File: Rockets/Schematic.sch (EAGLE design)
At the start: 9 parts, among them IC1 LM2937

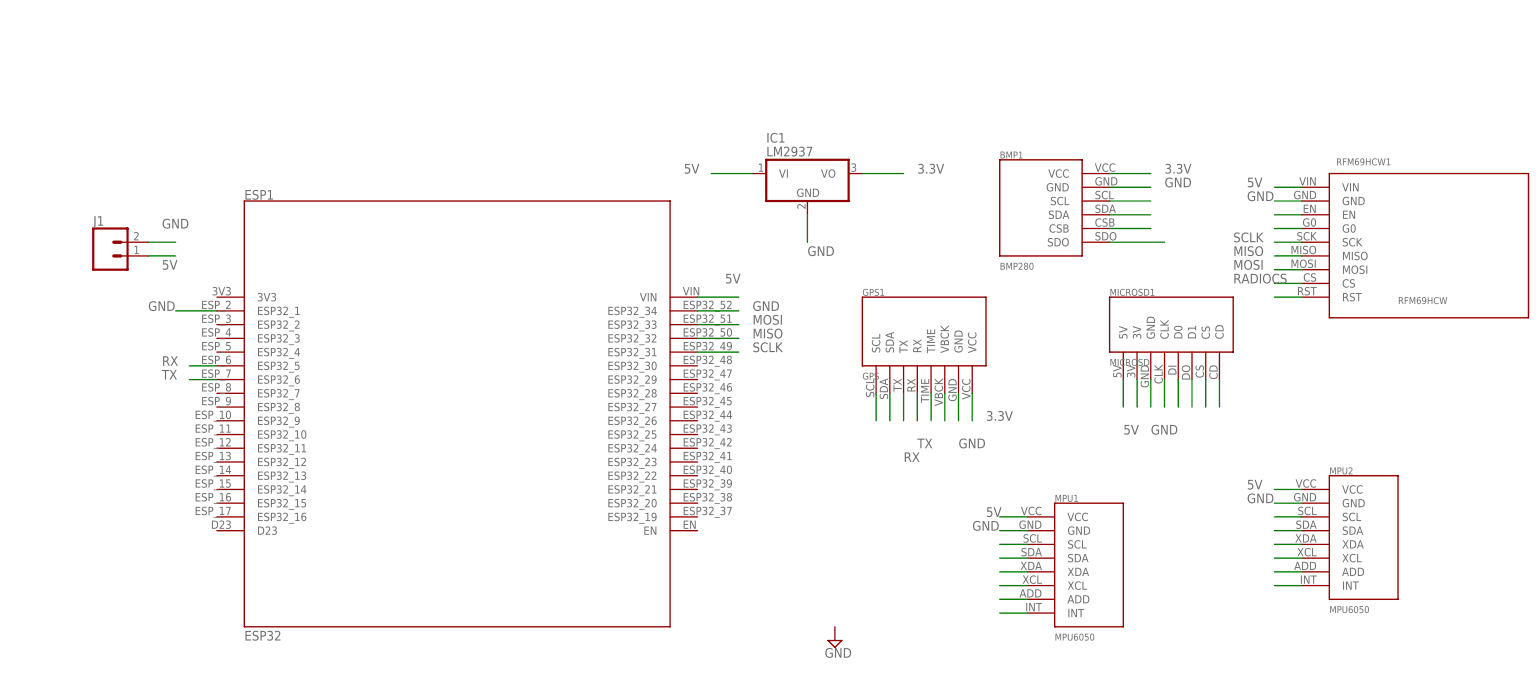
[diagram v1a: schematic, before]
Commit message: Everthing added needs resistors
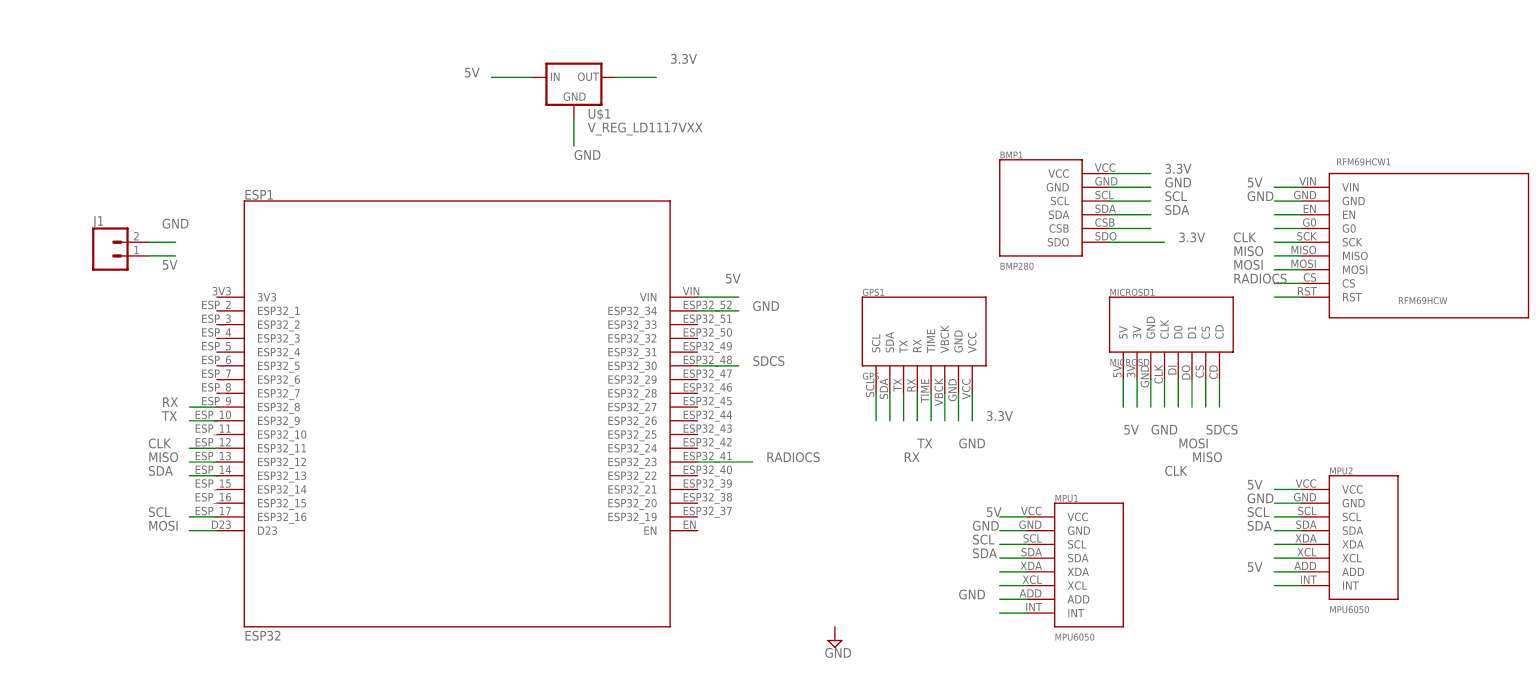
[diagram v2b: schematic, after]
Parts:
- removed IC1: LM2937, linear:LM2937
- added U$1: V_REG_LD1117VXX, SparkFun-IC-Power:V_REG_LD1117VXX
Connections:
- removed net N$19: MICROSD1.CS
- removed net N$20: MICROSD1.D1
- removed net N$21: MICROSD1.CLK
- removed net N$22: MICROSD1.D0
- removed net N$23: MPU1.SCL
- removed net N$26: MPU1.SDA
- removed net N$29: MPU1.ADD
- removed net N$33: MPU2.SCL
- removed net N$34: MPU2.SDA
- removed net N$38: MPU2.ADD
- removed net N$5: BMP1.SCL
- removed net N$6: BMP1.SDA
- removed net N$8: BMP1.SDO
- removed net SCLK: ESP1.ESP32_31, RFM69HCW1.SCK
- new net CLK: ESP1.ESP32_11, MICROSD1.CLK, RFM69HCW1.SCK
- new net SCL: BMP1.SCL, ESP1.ESP32_16, MPU1.SCL, MPU2.SCL
- new net SDA: BMP1.SDA, ESP1.ESP32_13, MPU1.SDA, MPU2.SDA
- new net SDCS: ESP1.ESP32_30, MICROSD1.CS
- net 3.3V: now also BMP1.SDO, U$1.OUT; no longer IC1.VO
- net 5V: now also MPU2.ADD, U$1.IN; no longer IC1.VI
- net GND: now also MPU1.ADD, U$1.GND; no longer ESP1.ESP32_1, IC1.GND
- net MISO: now also ESP1.ESP32_12, MICROSD1.D1; no longer ESP1.ESP32_32
- net MOSI: now also ESP1.D23, MICROSD1.D0; no longer ESP1.ESP32_33
- net RADIOCS: now also ESP1.ESP32_23
- net RX: now also ESP1.ESP32_8; no longer ESP1.ESP32_5
- net TX: now also ESP1.ESP32_9; no longer ESP1.ESP32_6

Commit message: Mk1 completed?
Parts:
- removed RFM69HCW1: RFM69HCW, awesome:RFM69HCW
- added C1, C2, C3, C4, C5, C6: 0.1uF, SparkFun-Capacitors:0.1UF-KIT-EZ-50V-20%
- added D1: (no value), SparkFun-LED:LED-3MM-NO_SILK
- added R1, R2, R3, R4, R5, R7: (no value), SparkFun-Resistors:RESISTORAXIAL-0.3
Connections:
- removed net N$18: MICROSD1.CD
- removed net N$9: RFM69HCW1.RST
- new net N$1: ESP1.ESP32_11, R3.1
- new net N$2: D1.A, ESP1.ESP32_27
- new net SDCD: ESP1.ESP32_24, MICROSD1.CD
- net 3.3V: now also C4.1, C6.1, R1.2, R7.2
- net 5V: now also C1.1, C2.1, C3.2, C5.2; no longer RFM69HCW1.VIN
- net CLK: now also R3.2; no longer ESP1.ESP32_11, RFM69HCW1.SCK
- net GND: now also C1.2, C2.2, C3.1, C4.2, C5.1, C6.2, R4.1; no longer RFM69HCW1.GND
- net MISO: now also R5.2; no longer MICROSD1.D1, RFM69HCW1.MISO
- net MOSI: now also R2.1, R2.2; no longer RFM69HCW1.MOSI
- net N$3: now also D1.C, R4.2; no longer RFM69HCW1.EN
- net N$4: now also MICROSD1.D1, R5.1; no longer RFM69HCW1.G0
- net RADIOCS: no longer RFM69HCW1.CS
- net SCL: now also R1.1
- net SDA: now also R7.1
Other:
- moved on the sheet: ESP1, GPS1

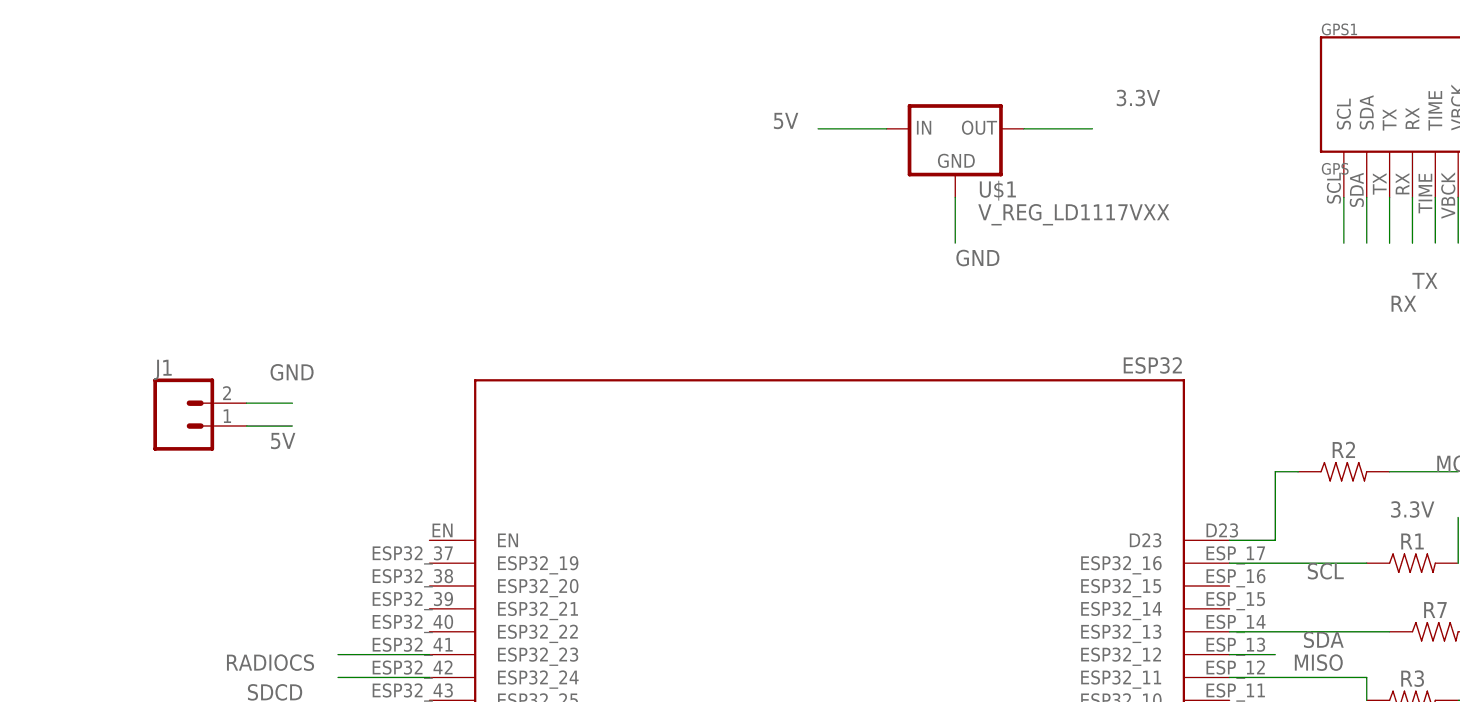
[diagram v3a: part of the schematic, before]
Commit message: Updated the schematics from discord zip
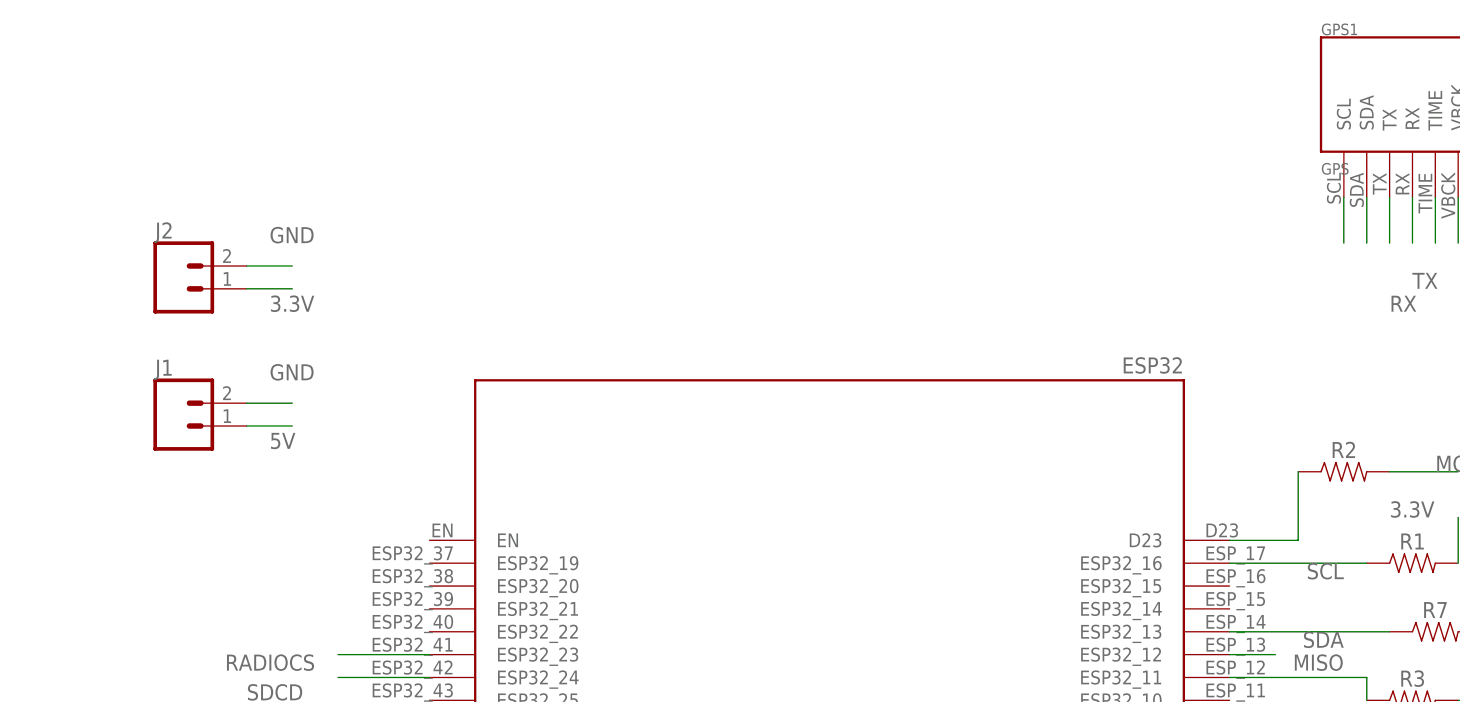
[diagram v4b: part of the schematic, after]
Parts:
- removed U$1: V_REG_LD1117VXX, SparkFun-IC-Power:V_REG_LD1117VXX
- added J2: (no value), SparkFun-Connectors:CONN_02
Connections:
- new net N$5: ESP1.D23, R2.1
- net 3.3V: now also J2.1; no longer U$1.OUT
- net 5V: no longer U$1.IN
- net GND: now also J2.2; no longer U$1.GND
- net MOSI: no longer ESP1.D23, R2.1
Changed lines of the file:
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@@
 <part name="J1" library="SparkFun-Connectors" deviceset="CONN_02" device=""/>
 <part name="BMP1" library="awesome" deviceset="BMP280" device=""/>
-<part name="U$1" library="SparkFun-IC-Power" deviceset="V_REG_LD1117VXX" device=""/>
 <part name="D1" library="SparkFun-LED" deviceset="LED" device="-3MM-NO_SILK"/>
 <part name="R1" library="SparkFun-Resistors" deviceset="RESISTOR" device="AXIAL-0.3" value=" "/>
@@
 <part name="R4" library="SparkFun-Resistors" deviceset="RESISTOR" device="AXIAL-0.3" value=" "/>
 <part name="R5" library="SparkFun-Resistors" deviceset="RESISTOR" device="AXIAL-0.3" value=" "/>
+<part name="J2" library="SparkFun-Connectors" deviceset="CONN_02" device=""/>
 </parts>
 <sheets>
@@
 <attribute name="VALUE" x="101.6" y="78.74" size="1.27" layer="96"/>
 </instance>
-<instance part="U$1" gate="G$1" x="22.86" y="114.3" smashed="yes">
-<attribute name="NAME" x="25.4" y="106.68" size="1.778" layer="95"/>
-<attribute name="VALUE" x="25.4" y="104.14" size="1.778" layer="96"/>
-</instance>
 <instance part="D1" gate="D1" x="-73.66" y="40.64" smashed="yes">
 <attribute name="NAME" x="-77.089" y="36.068" size="1.778" layer="95" font="vector" rot="R90"/>
@@
 <attribute name="NAME" x="152.4" y="47.244" size="1.778" layer="95" font="vector" align="bottom-center"/>
 <attribute name="VALUE" x="152.4" y="44.196" size="1.778" layer="96" font="vector" align="top-center"/>
+</instance>
+<instance part="J2" gate="G$1" x="-63.5" y="96.52" smashed="yes">
+<attribute name="VALUE" x="-66.04" y="91.694" size="1.778" layer="96" font="vector"/>
+<attribute name="NAME" x="-66.04" y="102.108" size="1.778" layer="95" font="vector"/>
 </instance>
 </instances>
@@
 <wire x1="-55.88" y1="81.28" x2="-50.8" y2="81.28" width="0.1524" layer="91"/>
 <label x="-53.34" y="78.74" size="1.778" layer="95"/>
-</segment>
-<segment>
-<pinref part="U$1" gate="G$1" pin="IN"/>
-<wire x1="15.24" y1="114.3" x2="7.62" y2="114.3" width="0.1524" layer="91"/>
-<label x="2.54" y="114.3" size="1.778" layer="95"/>
 </segment>
 <segment>
@@
 <wire x1="-55.88" y1="83.82" x2="-50.8" y2="83.82" width="0.1524" layer="91"/>
 <label x="-53.34" y="86.36" size="1.778" layer="95"/>
-</segment>
-<segment>
-<pinref part="U$1" gate="G$1" pin="GND"/>
-<wire x1="22.86" y1="106.68" x2="22.86" y2="101.6" width="0.1524" layer="91"/>
-<label x="22.86" y="99.06" size="1.778" layer="95"/>
 </segment>
 <segment>
@@
 <label x="86.36" y="86.36" size="1.778" layer="95"/>
 </segment>
+<segment>
+<pinref part="J2" gate="G$1" pin="2"/>
+<wire x1="-55.88" y1="99.06" x2="-50.8" y2="99.06" width="0.1524" layer="91"/>
+<label x="-53.34" y="101.6" size="1.778" layer="95"/>
+</segment>
 </net>
 <net name="CLK" class="0">
@@
 <net name="MOSI" class="0">
 <segment>
-<pinref part="R2" gate="G$1" pin="1"/>
-<wire x1="58.42" y1="68.58" x2="58.42" y2="76.2" width="0.1524" layer="91"/>
-<wire x1="58.42" y1="76.2" x2="60.96" y2="76.2" width="0.1524" layer="91"/>
-<pinref part="ESP1" gate="G$1" pin="D23"/>
-<wire x1="53.34" y1="68.58" x2="58.42" y2="68.58" width="0.1524" layer="91"/>
-</segment>
-<segment>
 <pinref part="MICROSD1" gate="G$1" pin="D0"/>
 <wire x1="134.62" y1="58.42" x2="134.62" y2="53.34" width="0.1524" layer="91"/>
@@
 </net>
 <net name="3.3V" class="0">
-<segment>
-<pinref part="U$1" gate="G$1" pin="OUT"/>
-<wire x1="30.48" y1="114.3" x2="38.1" y2="114.3" width="0.1524" layer="91"/>
-<label x="40.64" y="116.84" size="1.778" layer="95"/>
-</segment>
 <segment>
 <pinref part="BMP1" gate="G$1" pin="SDO"/>
@@
 <label x="96.52" y="104.14" size="1.778" layer="95"/>
 </segment>
+<segment>
+<pinref part="J2" gate="G$1" pin="1"/>
+<wire x1="-55.88" y1="96.52" x2="-50.8" y2="96.52" width="0.1524" layer="91"/>
+<label x="-53.34" y="93.98" size="1.778" layer="95"/>
+</segment>
 </net>
 <net name="N$12" class="0">
@@
 </segment>
 </net>
+<net name="N$5" class="0">
+<segment>
+<pinref part="ESP1" gate="G$1" pin="D23"/>
+<pinref part="R2" gate="G$1" pin="1"/>
+<wire x1="53.34" y1="68.58" x2="60.96" y2="68.58" width="0.1524" layer="91"/>
+<wire x1="60.96" y1="68.58" x2="60.96" y2="76.2" width="0.1524" layer="91"/>
+</segment>
+</net>
